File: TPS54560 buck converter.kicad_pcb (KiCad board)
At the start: 2 copper layers, 36.5 x 31 mm, 27 parts, among them J1 IN, J2 OUT, U1 TPS54560

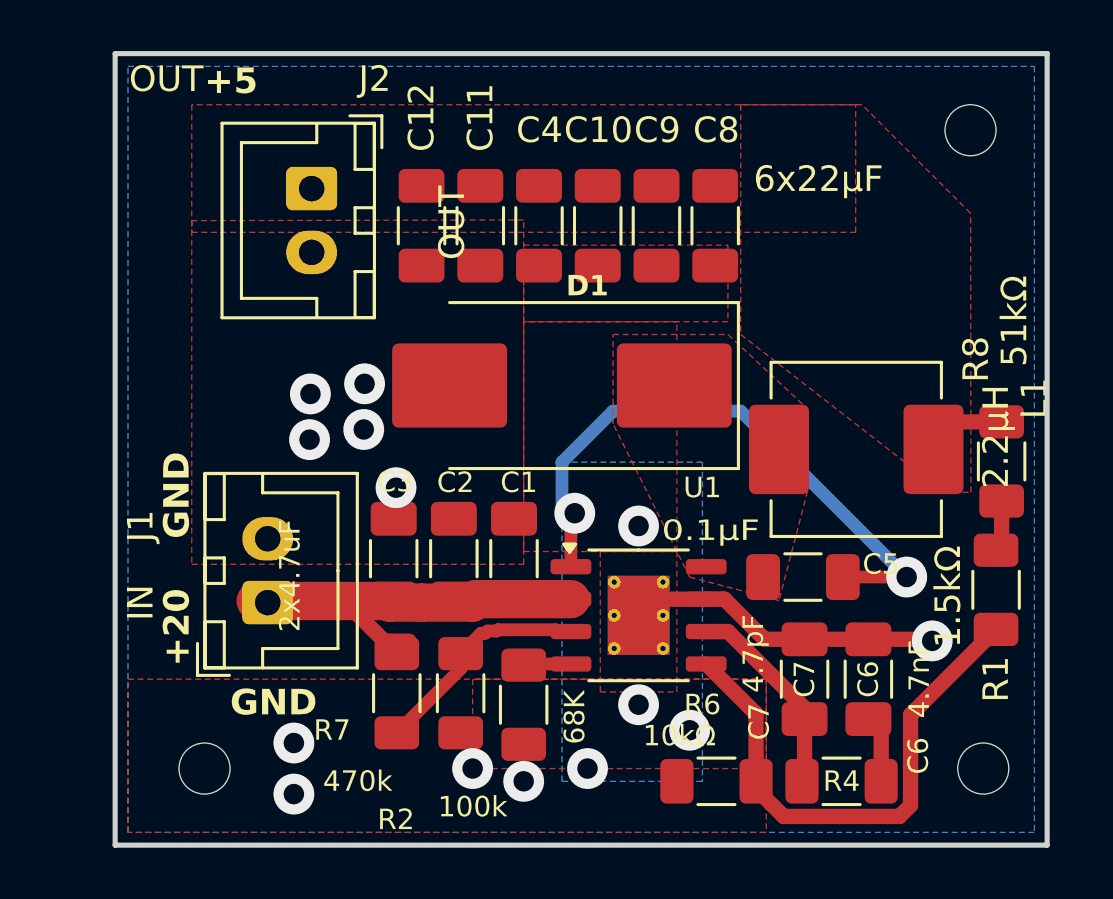
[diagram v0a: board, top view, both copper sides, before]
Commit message: Replace diode with TO-220 diode
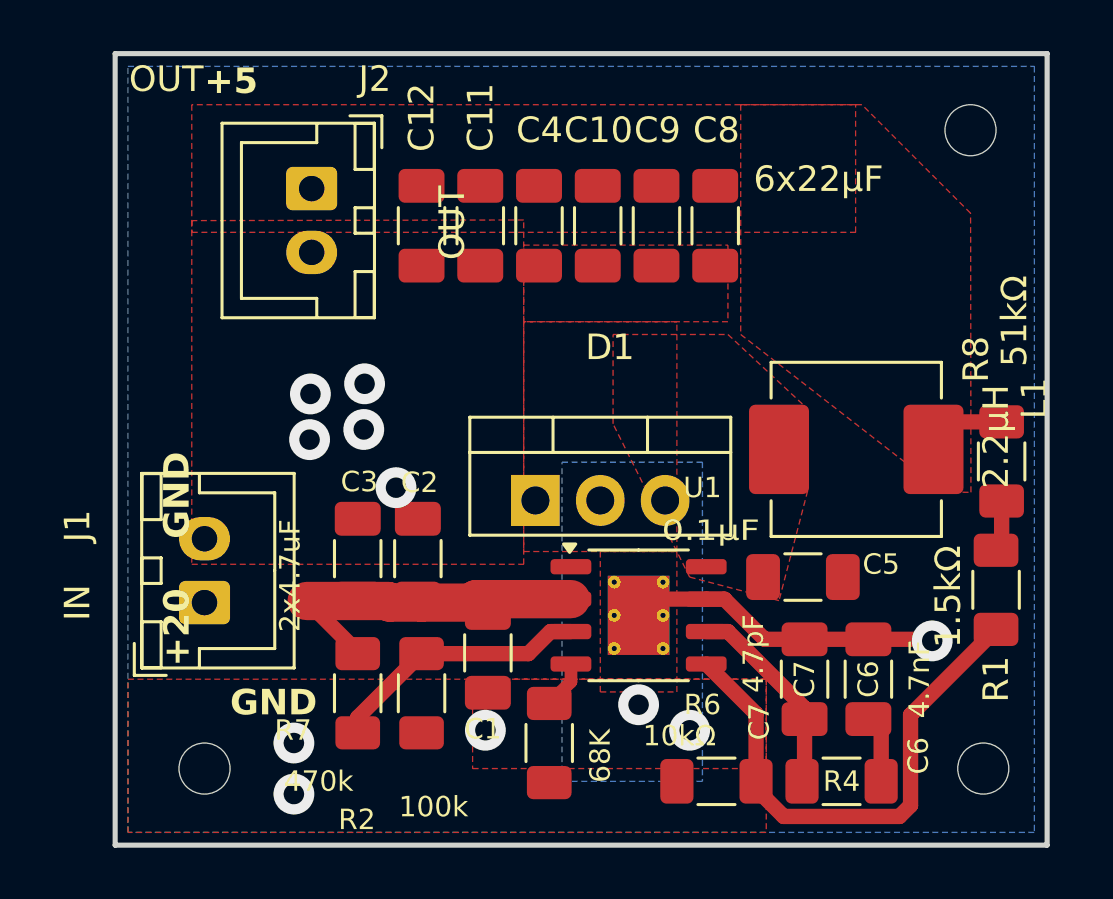
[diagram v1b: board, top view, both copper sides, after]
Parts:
- D1: value B530C 13 F -> Schottky_MBR20100CT; footprint Diode_SMD:D_SMC_Handsoldering -> Package_TO_SOT_THT:TO-220-3_Vertical
- moved D1 4.62 mm to (110.5, 83.0), turned to 0 degrees
- moved C1 3.83 mm to (108.6, 89.0), turned to -90 degrees
- moved J1 2.47 mm to (97.5, 87.0)
- moved R3 1.80 mm to (111.0, 92.5)
- moved R2 1.53 mm to (106.0, 90.5)
- moved R7 1.53 mm to (103.5, 90.5)
- moved C2 1.41 mm to (105.9, 85.3)
- moved C3 1.41 mm to (103.5, 85.3)
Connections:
- D1 pad 1: /SW -> GND
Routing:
- net Net-(U1-Boot): track 23.2 -> 0.00 mm, vias 2 -> 0
- net +20V: track 17.1 -> 14.8 mm
- net Net-(U1-EN): track 8.33 -> 10.3 mm
- net GND: vias 14 -> 11

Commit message: Cleans up board
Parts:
- moved C10 2.50 mm to (113.4, 74.7)
- moved C11 2.50 mm to (108.8, 74.7)
- moved C12 2.50 mm to (106.5, 74.7)
- moved C4 2.50 mm to (111.1, 74.7)
- moved C8 2.50 mm to (118.0, 74.7)
- moved C9 2.50 mm to (115.7, 74.7)
- moved J2 2.46 mm to (102.0, 73.2)
- moved J1 0.86 mm to (98.4, 87.0)
- moved C2 0.33 mm to (106.2, 85.3)
- moved C3 0.33 mm to (103.8, 85.3)
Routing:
- net Net-(U1-Boot): track 0.00 -> 18.5 mm, vias 0 -> 2
- net +20V: track 14.8 -> 18.0 mm
- net GND: vias 11 -> 14
